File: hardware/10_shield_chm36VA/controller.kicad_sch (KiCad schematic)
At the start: 36 parts, among them Q1 IRLL2705PBF, Q2 IRLL2705PBF, Q3 BSS138BKS, Q4 IRLL2705PBF, Q5 IRLL2705PBF, Q6 IRLL2705PBF, Q7 IRLL2705PBF, Q8 IRLL2705PBF, Q9 IRLL2705PBF, U1 L7809, U2 AM26LV32xNS, U3 CNY17-1

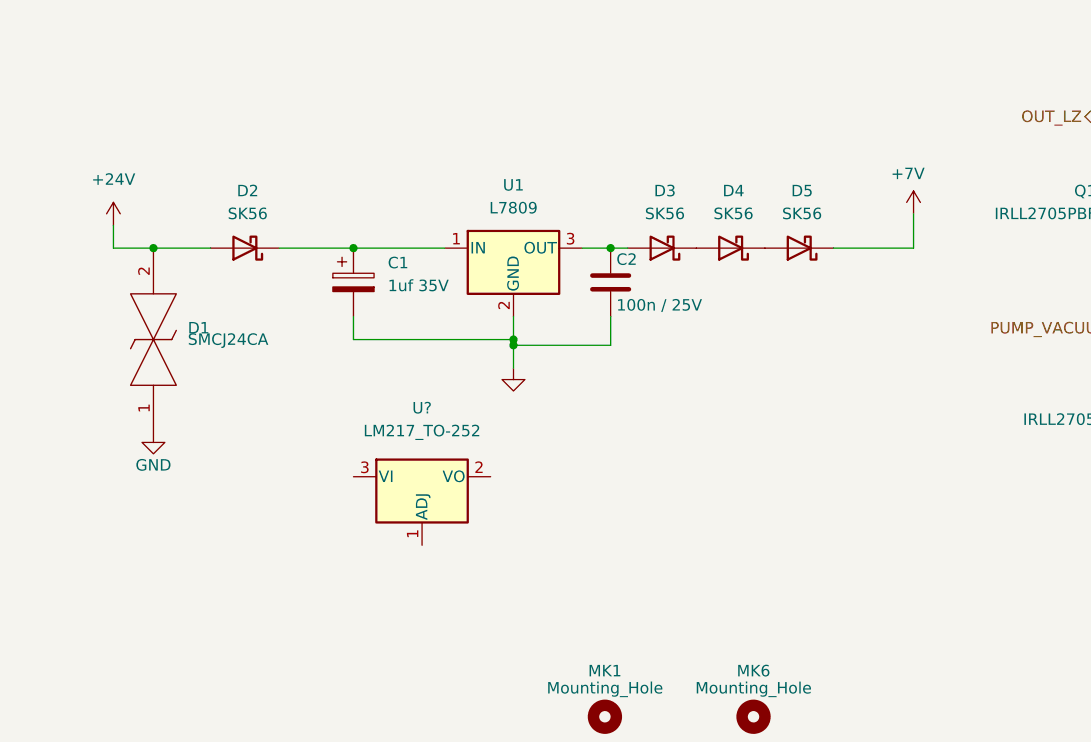
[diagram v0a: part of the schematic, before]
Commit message: Fixes in PCB
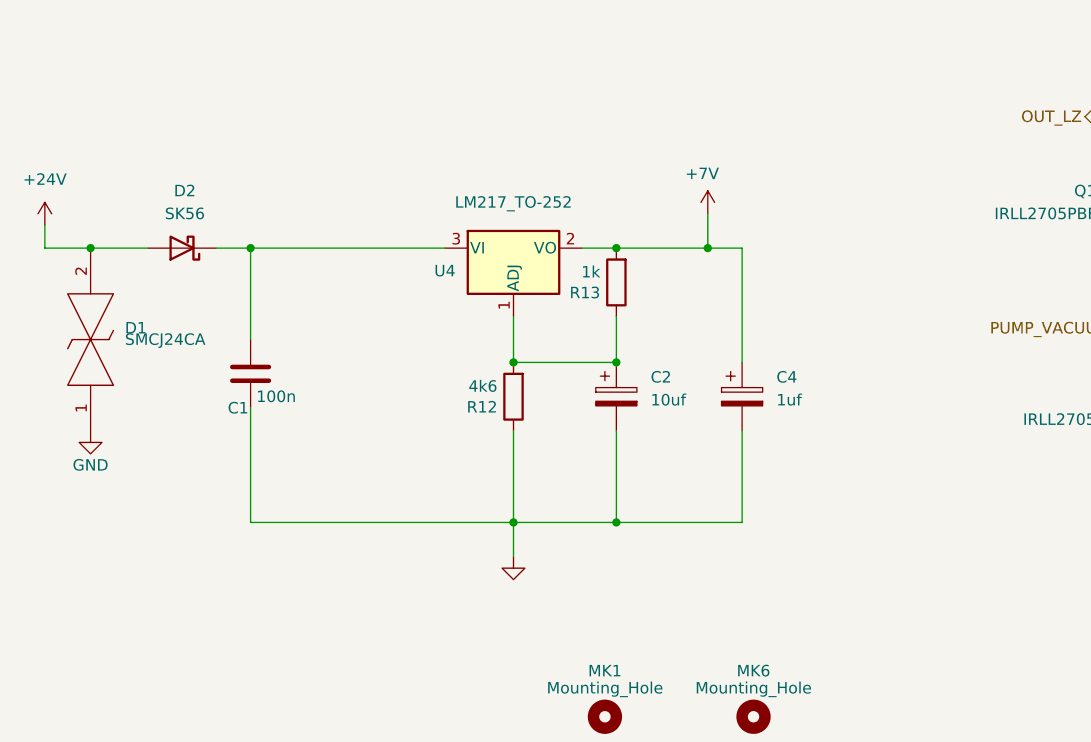
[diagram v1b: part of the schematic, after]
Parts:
- removed C1: 1uf 35V, Capacitor_Tantalum_SMD:CP_EIA-3216-18_Kemet-A, symbol Device:C_Polarized
- removed C2: 100n / 25V, Capacitor_SMD:C_0603_1608Metric, symbol mfc_base_lib:C
- removed D3, D4, D5: SK56, Diode_SMD:D_SMB, symbol Device:D_Schottky
- removed U1: L7809, Package_TO_SOT_SMD:TO-263-2, symbol Regulator_Linear:L7809
- added C1: 100n, Capacitor_SMD:C_0603_1608Metric, symbol mfc_base_lib:C
- added C2: 10uf, Capacitor_Tantalum_SMD:CP_EIA-3528-21_Kemet-B, symbol Device:C_Polarized
- added C4: 1uf, Capacitor_Tantalum_SMD:CP_EIA-3528-21_Kemet-B, symbol Device:C_Polarized
- added R12: 4k6, Resistor_SMD:R_0603_1608Metric, symbol Uni_Printer-rescue:R-Device
- added R13: 1k, Resistor_SMD:R_0603_1608Metric, symbol Uni_Printer-rescue:R-Device
- gave numbers to parts that had none: 1
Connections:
- net +7V: now also U4.2 (VO), C4.1, R13.2
- net GND: now also C1.2, C2.2, C4.2, R12.1
- net at U4.1 (ADJ): now also C2.1, R12.2, R13.1
- net at U4.3 (VI): now also D2.1 (K), C1.1
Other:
- moved on the sheet: D1, D2, U4

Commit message: Prepared for first prototype
Signed-off-by: Jarosław Karwik <jaroslaw.karwik@gmail.com>
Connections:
- net VSUP: now also C1.1, D2.1 (K), U4.3 (VI)
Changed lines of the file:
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@@
     (stroke (width 0) (type default) (color 0 0 0 0))
+  )
+  (label "VSUP" (at 71.12 133.35 0)
+    (effects (font (size 1.27 1.27)) (justify left bottom))
   )
   (label "VSUP" (at 226.695 239.395 0)
